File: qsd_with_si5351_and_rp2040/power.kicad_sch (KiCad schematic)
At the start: 9 parts, among them J201 Conn_01x02, J202 Conn_01x03, J203 Conn_01x03, U201 AP1117-33

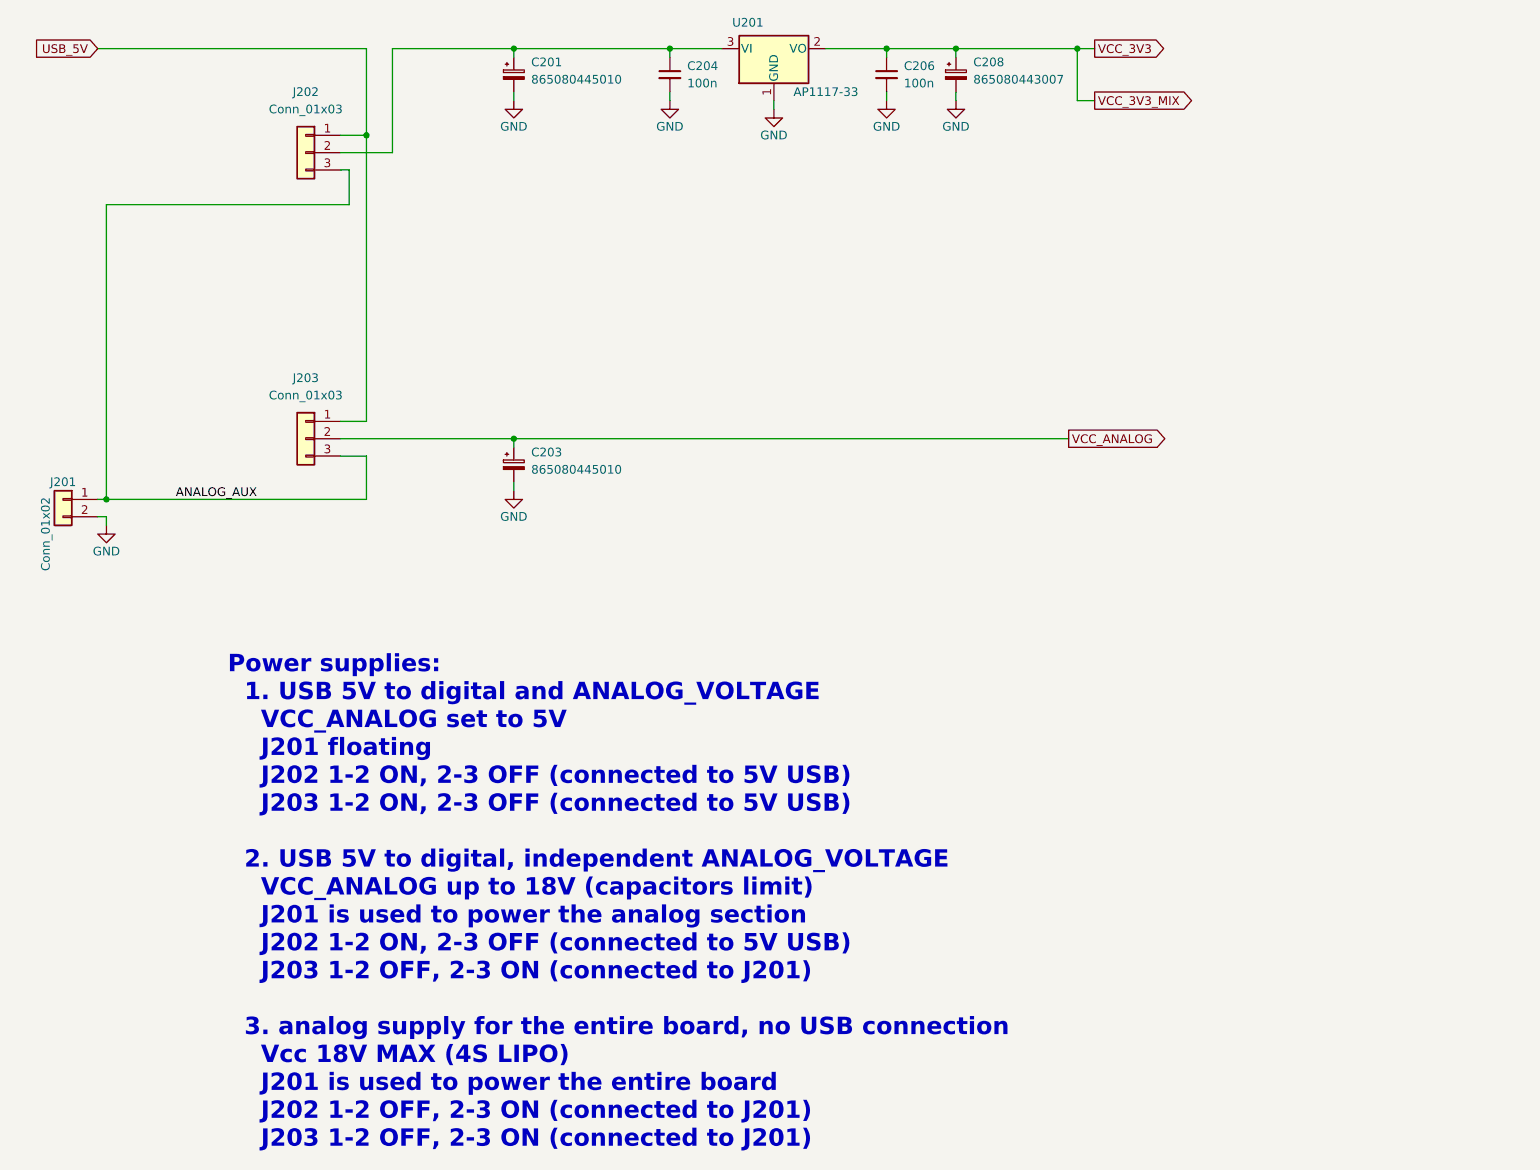
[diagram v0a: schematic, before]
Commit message: version with stackable connector
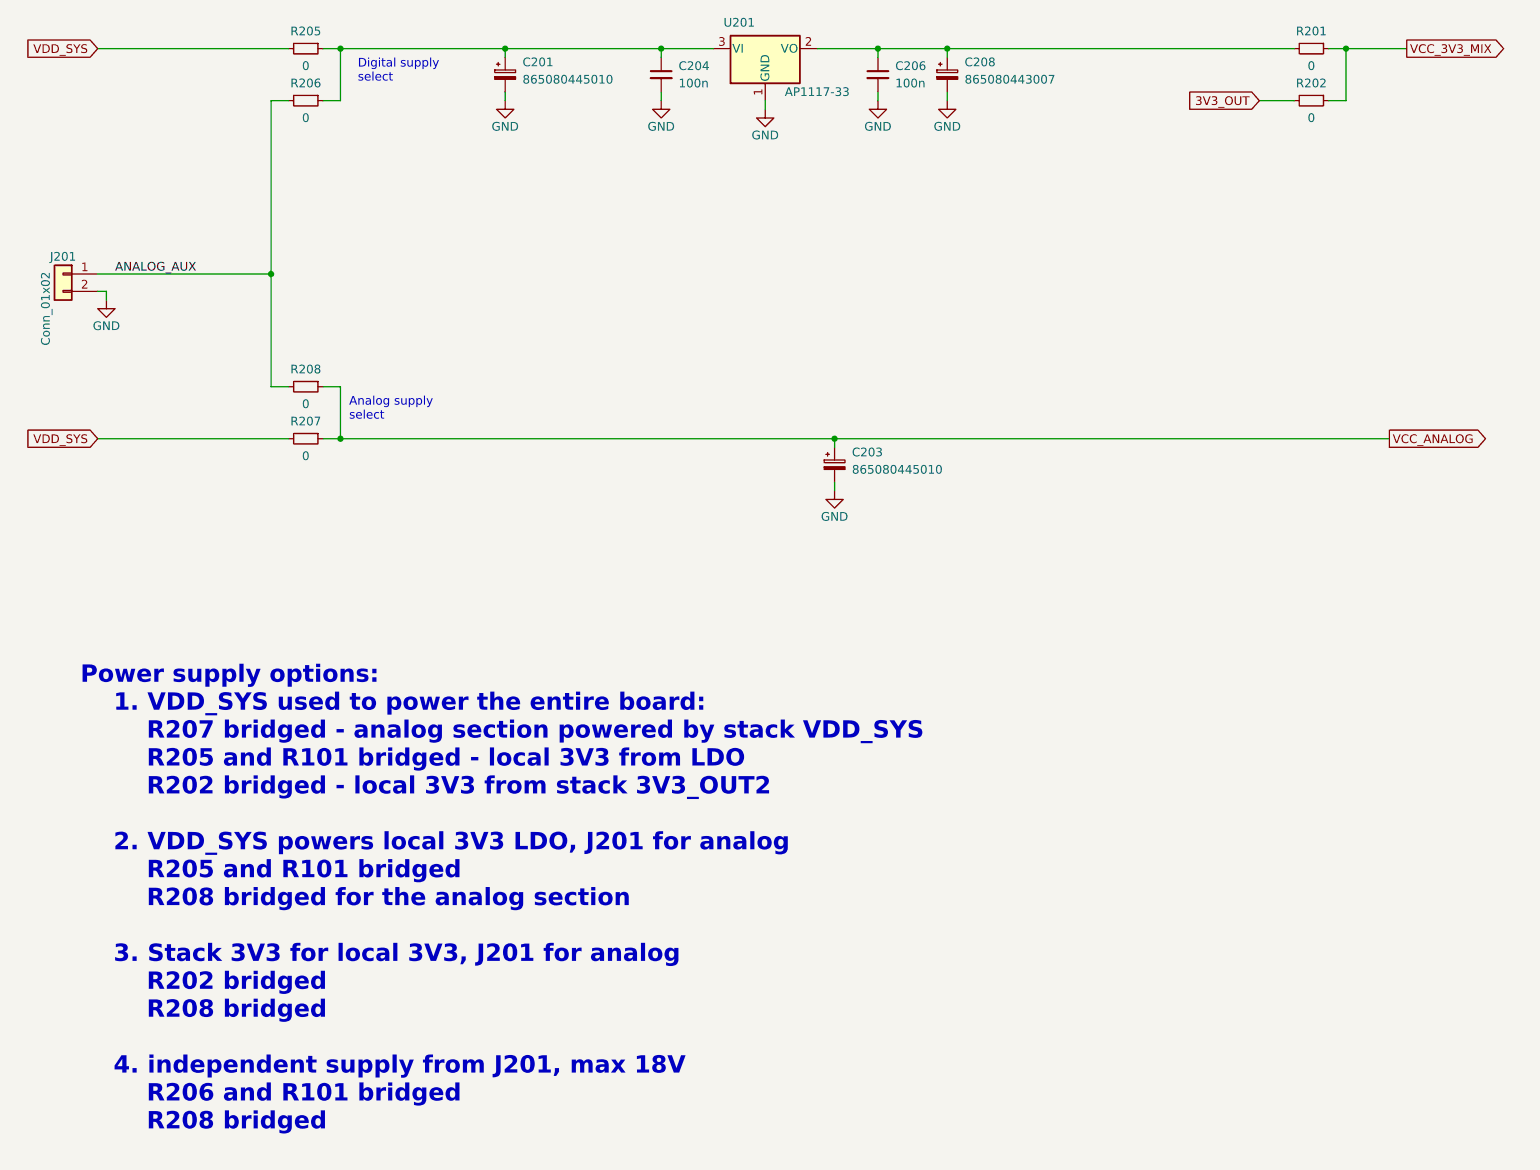
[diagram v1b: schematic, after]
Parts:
- removed J202, J203: Conn_01x03, Connector_PinHeader_2.54mm:PinHeader_1x03_P2.54mm_Vertical, symbol Connector_Generic:Conn_01x03
- added R201, R202, R205, R206, R207, R208: 0, Resistor_SMD:R_0805_2012Metric_Pad1.20x1.40mm_HandSolder, symbol Device:R_Small
- J201: footprint Connector_PinSocket_2.54mm:PinSocket_1x02_P2.54mm_Vertical -> Connector_PinHeader_2.54mm:PinHeader_1x02_P2.54mm_Vertical
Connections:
- net ANALOG_AUX: now also R206.2, R208.2
- net VCC_ANALOG: now also R207.1, R208.1
- net at C201.1, C204.1, U201.3 (VI): now also R205.1, R206.1
- net VCC_3V3: no longer names the net of C206.1, C208.1, U201.2 (VO)
- net VCC_3V3: now also R201.2
- new net 3V3_OUT: R202.2
- new net VCC_3V3_MIX: R201.1, R202.1
- new net VDD_SYS: R205.2, R207.2
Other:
- note added: "Analog supply select"
- note added: "Digital supply select"
- note added: "Power supply options: 1. VDD_SYS used to power the entire board: R207 bridged - analog section powered by stack VDD_SYS R205 and R101 bridged - local 3V3 from LDO R202 bridged - local 3V3 from stack 3V3_OUT2 2. VDD_SYS powers local 3V3 LDO, J201 for analog R205 and R101 bridged R208 bridged for the analog section 3. Stack 3V3 for local 3V3, J201 for analog R202 bridged R208 bridged 4. independent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"
- note removed: "Power supplies: 1. USB 5V to digital and ANALOG_VOLTAGE VCC_ANALOG set to 5V J201 floating J202 1-2 ON, 2-3 OFF (connected to 5V USB) J203 1-2 ON, 2-3 OFF (connected to 5V USB) 2. USB 5V to digital, independent ANALOG_VOLTAGE VCC_ANALOG up to 18V (capacitors limit) J201 is used to power the analog section J202 1-2 ON, 2-3 OFF (connected to 5V USB) J203 1-2 OFF, 2-3 ON (connected to J201) 3. analo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"
- moved on the sheet: C201, C203, C204, C206, C208, J201, U201
